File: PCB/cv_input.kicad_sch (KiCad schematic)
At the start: 4 parts

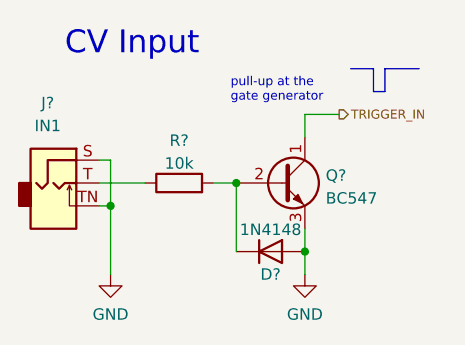
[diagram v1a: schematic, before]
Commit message: :hammer: Change inputs to the intended 3 manual 1 CV inputs
There was a mistake when creating the hierarchical sheets leading to 3 CV
inputs and one manual input instead of the other way around.
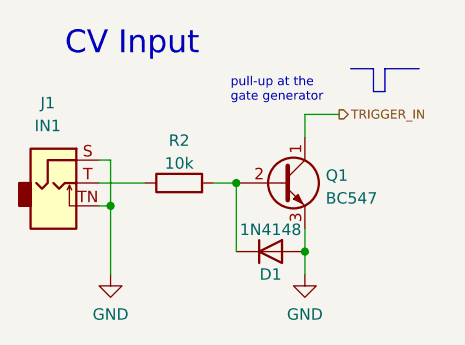
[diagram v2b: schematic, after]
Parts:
- gave numbers to parts that had none: 4
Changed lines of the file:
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@@
   (symbol (lib_id "power:GND") (at 58.42 52.07 0) (unit 1)
     (in_bom yes) (on_board yes) (dnp no) (fields_autoplaced)
-    (property "Reference" "#PWR?" (at 58.42 58.42 0)
+    (property "Reference" "#PWR04" (at 58.42 58.42 0)
       (effects (font (size 1.27 1.27)) hide)
     )
@@
     (instances
       (project "manual-gate-trigger-source"
-        (path "/64d6412c-bfad-42df-9ed7-bcc6cbff0470/fb6762b1-53b2-4253-9ea8-56c83353230a"
-          (reference "#PWR?") (unit 1)
-        )
-        (path "/64d6412c-bfad-42df-9ed7-bcc6cbff0470/199ac3ae-221a-47d5-9e9f-e559d819f98b"
-          (reference "#PWR?") (unit 1)
-        )
-        (path "/64d6412c-bfad-42df-9ed7-bcc6cbff0470/dfca1d14-f5c9-49c7-bdd1-db3f878ec903"
-          (reference "#PWR?") (unit 1)
+        (path "/64d6412c-bfad-42df-9ed7-bcc6cbff0470/fd0933f7-8da4-4985-a361-ff361c3b6a05"
+          (reference "#PWR04") (unit 1)
         )
       )
@@
   (symbol (lib_id "Device:R") (at 44.45 41.91 90) (unit 1)
     (in_bom yes) (on_board yes) (dnp no) (fields_autoplaced)
-    (property "Reference" "R?" (at 44.45 37.1942 90)
+    (property "Reference" "R2" (at 44.45 37.1942 90)
       (effects (font (size 1.27 1.27)))
     )
@@
     (instances
       (project "manual-gate-trigger-source"
-        (path "/64d6412c-bfad-42df-9ed7-bcc6cbff0470/fb6762b1-53b2-4253-9ea8-56c83353230a"
-          (reference "R?") (unit 1)
-        )
-        (path "/64d6412c-bfad-42df-9ed7-bcc6cbff0470/199ac3ae-221a-47d5-9e9f-e559d819f98b"
-          (reference "R?") (unit 1)
-        )
-        (path "/64d6412c-bfad-42df-9ed7-bcc6cbff0470/dfca1d14-f5c9-49c7-bdd1-db3f878ec903"
-          (reference "R?") (unit 1)
+        (path "/64d6412c-bfad-42df-9ed7-bcc6cbff0470/fd0933f7-8da4-4985-a361-ff361c3b6a05"
+          (reference "R2") (unit 1)
         )
       )
@@
   (symbol (lib_id "Connector:AudioJack2_Ground_SwitchT") (at 30.48 41.91 0) (unit 1)
     (in_bom yes) (on_board yes) (dnp no) (fields_autoplaced)
-    (property "Reference" "J?" (at 29.845 33.02 0)
+    (property "Reference" "J1" (at 29.845 33.02 0)
       (effects (font (size 1.27 1.27)))
     )
@@
     (instances
       (project "manual-gate-trigger-source"
-        (path "/64d6412c-bfad-42df-9ed7-bcc6cbff0470/fb6762b1-53b2-4253-9ea8-56c83353230a"
-          (reference "J?") (unit 1)
-        )
-        (path "/64d6412c-bfad-42df-9ed7-bcc6cbff0470/199ac3ae-221a-47d5-9e9f-e559d819f98b"
-          (reference "J?") (unit 1)
-        )
-        (path "/64d6412c-bfad-42df-9ed7-bcc6cbff0470/dfca1d14-f5c9-49c7-bdd1-db3f878ec903"
-          (reference "J?") (unit 1)
+        (path "/64d6412c-bfad-42df-9ed7-bcc6cbff0470/fd0933f7-8da4-4985-a361-ff361c3b6a05"
+          (reference "J1") (unit 1)
         )
       )
@@
   (symbol (lib_id "Diode:1N4148") (at 54.61 49.53 0) (unit 1)
     (in_bom yes) (on_board yes) (dnp no)
-    (property "Reference" "D?" (at 54.61 52.07 0)
+    (property "Reference" "D1" (at 54.61 52.07 0)
       (effects (font (size 1.27 1.27)))
     )
@@
     (instances
       (project "manual-gate-trigger-source"
-        (path "/64d6412c-bfad-42df-9ed7-bcc6cbff0470/fb6762b1-53b2-4253-9ea8-56c83353230a"
-          (reference "D?") (unit 1)
-        )
-        (path "/64d6412c-bfad-42df-9ed7-bcc6cbff0470/199ac3ae-221a-47d5-9e9f-e559d819f98b"
-          (reference "D?") (unit 1)
-        )
-        (path "/64d6412c-bfad-42df-9ed7-bcc6cbff0470/dfca1d14-f5c9-49c7-bdd1-db3f878ec903"
-          (reference "D?") (unit 1)
+        (path "/64d6412c-bfad-42df-9ed7-bcc6cbff0470/fd0933f7-8da4-4985-a361-ff361c3b6a05"
+          (reference "D1") (unit 1)
         )
       )
@@
   (symbol (lib_id "Transistor_BJT:BC547") (at 55.88 41.91 0) (unit 1)
     (in_bom yes) (on_board yes) (dnp no) (fields_autoplaced)
-    (property "Reference" "Q?" (at 60.7314 41.0753 0)
+    (property "Reference" "Q1" (at 60.7314 41.0753 0)
       (effects (font (size 1.27 1.27)) (justify left))
     )
@@
     (instances
       (project "manual-gate-trigger-source"
-        (path "/64d6412c-bfad-42df-9ed7-bcc6cbff0470/fb6762b1-53b2-4253-9ea8-56c83353230a"
-          (reference "Q?") (unit 1)
-        )
-        (path "/64d6412c-bfad-42df-9ed7-bcc6cbff0470/199ac3ae-221a-47d5-9e9f-e559d819f98b"
-          (reference "Q?") (unit 1)
-        )
-        (path "/64d6412c-bfad-42df-9ed7-bcc6cbff0470/dfca1d14-f5c9-49c7-bdd1-db3f878ec903"
-          (reference "Q?") (unit 1)
+        (path "/64d6412c-bfad-42df-9ed7-bcc6cbff0470/fd0933f7-8da4-4985-a361-ff361c3b6a05"
+          (reference "Q1") (unit 1)
         )
       )
@@
   (symbol (lib_id "power:GND") (at 36.83 52.07 0) (unit 1)
     (in_bom yes) (on_board yes) (dnp no) (fields_autoplaced)
-    (property "Reference" "#PWR?" (at 36.83 58.42 0)
+    (property "Reference" "#PWR03" (at 36.83 58.42 0)
       (effects (font (size 1.27 1.27)) hide)
     )
@@
     (instances
       (project "manual-gate-trigger-source"
-        (path "/64d6412c-bfad-42df-9ed7-bcc6cbff0470/fb6762b1-53b2-4253-9ea8-56c83353230a"
-          (reference "#PWR?") (unit 1)
-        )
-        (path "/64d6412c-bfad-42df-9ed7-bcc6cbff0470/199ac3ae-221a-47d5-9e9f-e559d819f98b"
-          (reference "#PWR?") (unit 1)
-        )
-        (path "/64d6412c-bfad-42df-9ed7-bcc6cbff0470/dfca1d14-f5c9-49c7-bdd1-db3f878ec903"
-          (reference "#PWR?") (unit 1)
+        (path "/64d6412c-bfad-42df-9ed7-bcc6cbff0470/fd0933f7-8da4-4985-a361-ff361c3b6a05"
+          (reference "#PWR03") (unit 1)
         )
       )

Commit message: :wrench: Assign component designators
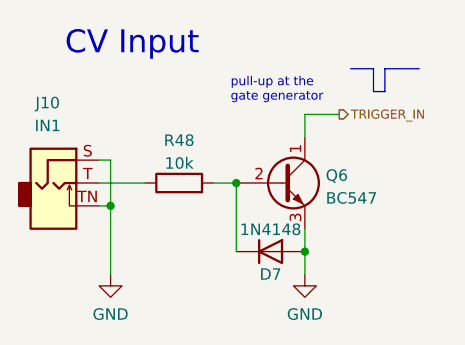
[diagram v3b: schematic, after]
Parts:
- renumbered D1 to D7, J1 to J10, Q1 to Q6, R2 to R48
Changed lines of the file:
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@@
   (symbol (lib_id "power:GND") (at 58.42 52.07 0) (unit 1)
     (in_bom yes) (on_board yes) (dnp no) (fields_autoplaced)
-    (property "Reference" "#PWR04" (at 58.42 58.42 0)
+    (property "Reference" "#PWR042" (at 58.42 58.42 0)
       (effects (font (size 1.27 1.27)) hide)
     )
@@
       (project "manual-gate-trigger-source"
         (path "/64d6412c-bfad-42df-9ed7-bcc6cbff0470/fd0933f7-8da4-4985-a361-ff361c3b6a05"
-          (reference "#PWR04") (unit 1)
+          (reference "#PWR042") (unit 1)
         )
       )
@@
   (symbol (lib_id "Device:R") (at 44.45 41.91 90) (unit 1)
     (in_bom yes) (on_board yes) (dnp no) (fields_autoplaced)
-    (property "Reference" "R2" (at 44.45 37.1942 90)
+    (property "Reference" "R48" (at 44.45 37.1942 90)
       (effects (font (size 1.27 1.27)))
     )
@@
       (project "manual-gate-trigger-source"
         (path "/64d6412c-bfad-42df-9ed7-bcc6cbff0470/fd0933f7-8da4-4985-a361-ff361c3b6a05"
-          (reference "R2") (unit 1)
+          (reference "R48") (unit 1)
         )
       )
@@
   (symbol (lib_id "Connector:AudioJack2_Ground_SwitchT") (at 30.48 41.91 0) (unit 1)
     (in_bom yes) (on_board yes) (dnp no) (fields_autoplaced)
-    (property "Reference" "J1" (at 29.845 33.02 0)
+    (property "Reference" "J10" (at 29.845 33.02 0)
       (effects (font (size 1.27 1.27)))
     )
@@
       (project "manual-gate-trigger-source"
         (path "/64d6412c-bfad-42df-9ed7-bcc6cbff0470/fd0933f7-8da4-4985-a361-ff361c3b6a05"
-          (reference "J1") (unit 1)
+          (reference "J10") (unit 1)
         )
       )
@@
   (symbol (lib_id "Diode:1N4148") (at 54.61 49.53 0) (unit 1)
     (in_bom yes) (on_board yes) (dnp no)
-    (property "Reference" "D1" (at 54.61 52.07 0)
+    (property "Reference" "D7" (at 54.61 52.07 0)
       (effects (font (size 1.27 1.27)))
     )
@@
       (project "manual-gate-trigger-source"
         (path "/64d6412c-bfad-42df-9ed7-bcc6cbff0470/fd0933f7-8da4-4985-a361-ff361c3b6a05"
-          (reference "D1") (unit 1)
+          (reference "D7") (unit 1)
         )
       )
@@
   (symbol (lib_id "Transistor_BJT:BC547") (at 55.88 41.91 0) (unit 1)
     (in_bom yes) (on_board yes) (dnp no) (fields_autoplaced)
-    (property "Reference" "Q1" (at 60.7314 41.0753 0)
+    (property "Reference" "Q6" (at 60.7314 41.0753 0)
       (effects (font (size 1.27 1.27)) (justify left))
     )
@@
       (project "manual-gate-trigger-source"
         (path "/64d6412c-bfad-42df-9ed7-bcc6cbff0470/fd0933f7-8da4-4985-a361-ff361c3b6a05"
-          (reference "Q1") (unit 1)
+          (reference "Q6") (unit 1)
         )
       )
@@
   (symbol (lib_id "power:GND") (at 36.83 52.07 0) (unit 1)
     (in_bom yes) (on_board yes) (dnp no) (fields_autoplaced)
-    (property "Reference" "#PWR03" (at 36.83 58.42 0)
+    (property "Reference" "#PWR041" (at 36.83 58.42 0)
       (effects (font (size 1.27 1.27)) hide)
     )
@@
       (project "manual-gate-trigger-source"
         (path "/64d6412c-bfad-42df-9ed7-bcc6cbff0470/fd0933f7-8da4-4985-a361-ff361c3b6a05"
-          (reference "#PWR03") (unit 1)
+          (reference "#PWR041") (unit 1)
         )
       )

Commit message: :wrench: Assign footprints to all symbols
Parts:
- R48: footprint (none) -> Resistor_THT:R_Axial_DIN0207_L6.3mm_D2.5mm_P7.62mm_Horizontal
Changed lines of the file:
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@@
       (effects (font (size 1.27 1.27)))
     )
-    (property "Footprint" "" (at 44.45 43.688 90)
+    (property "Footprint" "Resistor_THT:R_Axial_DIN0207_L6.3mm_D2.5mm_P7.62mm_Horizontal" (at 44.45 43.688 90)
       (effects (font (size 1.27 1.27)) hide)
     )

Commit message: :sparkles: Set PCB size and UI component placement
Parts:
- J10: footprint Connector_Audio:Jack_3.5mm_QingPu_WQP-PJ398SM_Vertical_CircularHoles -> moPsy:Jack_3.5mm_QingPu_WQP-PJ398SM_Vertical_CircularHoles_Centered
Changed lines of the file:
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@@
       (effects (font (size 1.27 1.27)))
     )
-    (property "Footprint" "Connector_Audio:Jack_3.5mm_QingPu_WQP-PJ398SM_Vertical_CircularHoles" (at 30.48 41.91 0)
+    (property "Footprint" "moPsy:Jack_3.5mm_QingPu_WQP-PJ398SM_Vertical_CircularHoles_Centered" (at 30.48 41.91 0)
       (effects (font (size 1.27 1.27)) hide)
     )

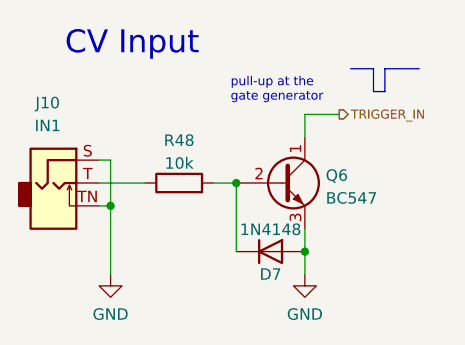
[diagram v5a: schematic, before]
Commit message: :hammer: Change transistor footprints to hand-solder variant
This fixes #56
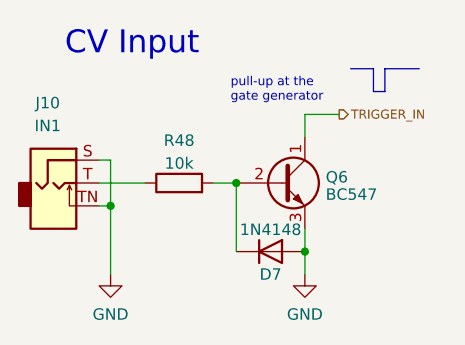
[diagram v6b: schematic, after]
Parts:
- Q6: footprint Package_TO_SOT_THT:TO-92_Inline -> Package_TO_SOT_THT:TO-92_HandSolder
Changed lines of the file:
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@@
   (symbol (lib_id "Transistor_BJT:BC547") (at 55.88 41.91 0) (unit 1)
     (in_bom yes) (on_board yes) (dnp no) (fields_autoplaced)
-    (property "Reference" "Q6" (at 60.7314 41.0753 0)
+    (property "Reference" "Q6" (at 60.7314 41.2663 0)
       (effects (font (size 1.27 1.27)) (justify left))
     )
-    (property "Value" "BC547" (at 60.7314 43.6122 0)
+    (property "Value" "BC547" (at 60.7314 43.1873 0)
       (effects (font (size 1.27 1.27)) (justify left))
     )
-    (property "Footprint" "Package_TO_SOT_THT:TO-92_Inline" (at 60.96 43.815 0)
+    (property "Footprint" "Package_TO_SOT_THT:TO-92_HandSolder" (at 60.96 43.815 0)
       (effects (font (size 1.27 1.27) italic) (justify left) hide)
     )

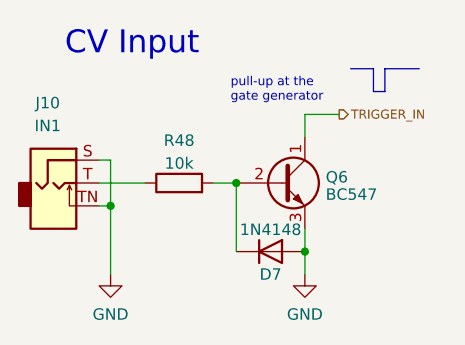
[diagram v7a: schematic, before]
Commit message: :memo: Geographically reannotate the PCB
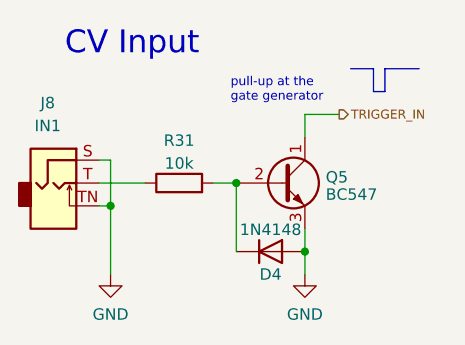
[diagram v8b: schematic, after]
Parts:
- renumbered D7 to D4, J10 to J8, Q6 to Q5, R48 to R31
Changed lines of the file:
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@@
   (symbol (lib_id "Device:R") (at 44.45 41.91 90) (unit 1)
     (in_bom yes) (on_board yes) (dnp no) (fields_autoplaced)
-    (property "Reference" "R48" (at 44.45 37.1942 90)
+    (property "Reference" "R31" (at 44.45 37.1942 90)
       (effects (font (size 1.27 1.27)))
     )
@@
       (project "manual-gate-trigger-source"
         (path "/64d6412c-bfad-42df-9ed7-bcc6cbff0470/fd0933f7-8da4-4985-a361-ff361c3b6a05"
-          (reference "R48") (unit 1)
+          (reference "R31") (unit 1)
         )
       )
@@
   (symbol (lib_id "Connector:AudioJack2_Ground_SwitchT") (at 30.48 41.91 0) (unit 1)
     (in_bom yes) (on_board yes) (dnp no) (fields_autoplaced)
-    (property "Reference" "J10" (at 29.845 33.02 0)
+    (property "Reference" "J8" (at 29.845 33.02 0)
       (effects (font (size 1.27 1.27)))
     )
@@
       (project "manual-gate-trigger-source"
         (path "/64d6412c-bfad-42df-9ed7-bcc6cbff0470/fd0933f7-8da4-4985-a361-ff361c3b6a05"
-          (reference "J10") (unit 1)
+          (reference "J8") (unit 1)
         )
       )
@@
   (symbol (lib_id "Diode:1N4148") (at 54.61 49.53 0) (unit 1)
     (in_bom yes) (on_board yes) (dnp no)
-    (property "Reference" "D7" (at 54.61 52.07 0)
+    (property "Reference" "D4" (at 54.61 52.07 0)
       (effects (font (size 1.27 1.27)))
     )
@@
       (project "manual-gate-trigger-source"
         (path "/64d6412c-bfad-42df-9ed7-bcc6cbff0470/fd0933f7-8da4-4985-a361-ff361c3b6a05"
-          (reference "D7") (unit 1)
+          (reference "D4") (unit 1)
         )
       )
@@
   (symbol (lib_id "Transistor_BJT:BC547") (at 55.88 41.91 0) (unit 1)
     (in_bom yes) (on_board yes) (dnp no) (fields_autoplaced)
-    (property "Reference" "Q6" (at 60.7314 41.2663 0)
+    (property "Reference" "Q5" (at 60.7314 41.2663 0)
       (effects (font (size 1.27 1.27)) (justify left))
     )
@@
       (project "manual-gate-trigger-source"
         (path "/64d6412c-bfad-42df-9ed7-bcc6cbff0470/fd0933f7-8da4-4985-a361-ff361c3b6a05"
-          (reference "Q6") (unit 1)
+          (reference "Q5") (unit 1)
         )
       )
